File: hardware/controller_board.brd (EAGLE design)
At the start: 86 x 70 mm, 94 parts, among them J1 USB-MICROA-AMPHENOL-10118192-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, J2 2.4K, J3 2.4K, J4 AVR_SPI_PRG_6-SMD, J7 FRSKY-GIMBAL-2X-SERVO-SMD, J8 FRSKY-GIMBAL-2X-SERVO-SMD, P1 TEST-POINT, P2 TEST-POINT, P3 TEST-POINT, P4 TEST-POINT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

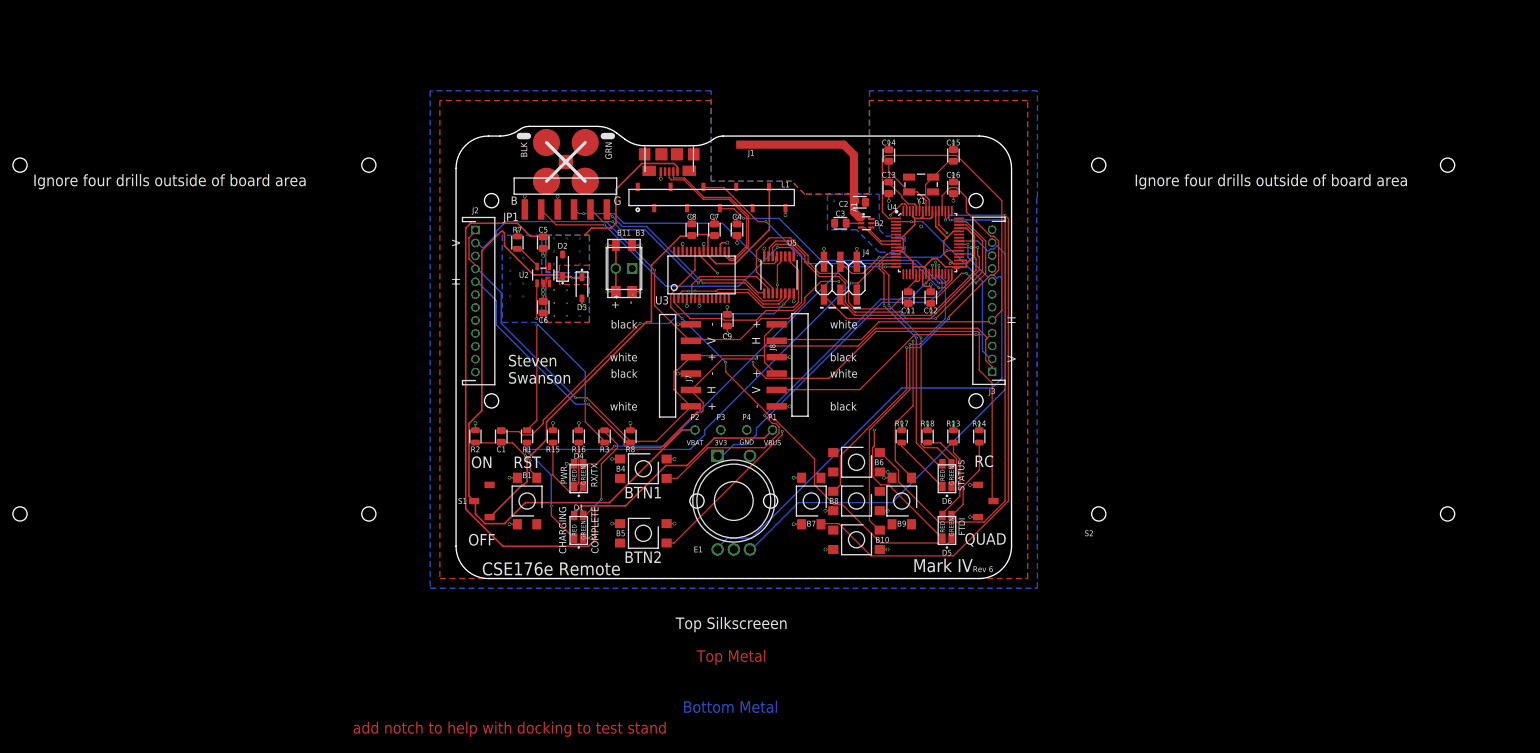
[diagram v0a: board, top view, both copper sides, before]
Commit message: reorg.  larger board.  More spacious.  Strain relief for the battery
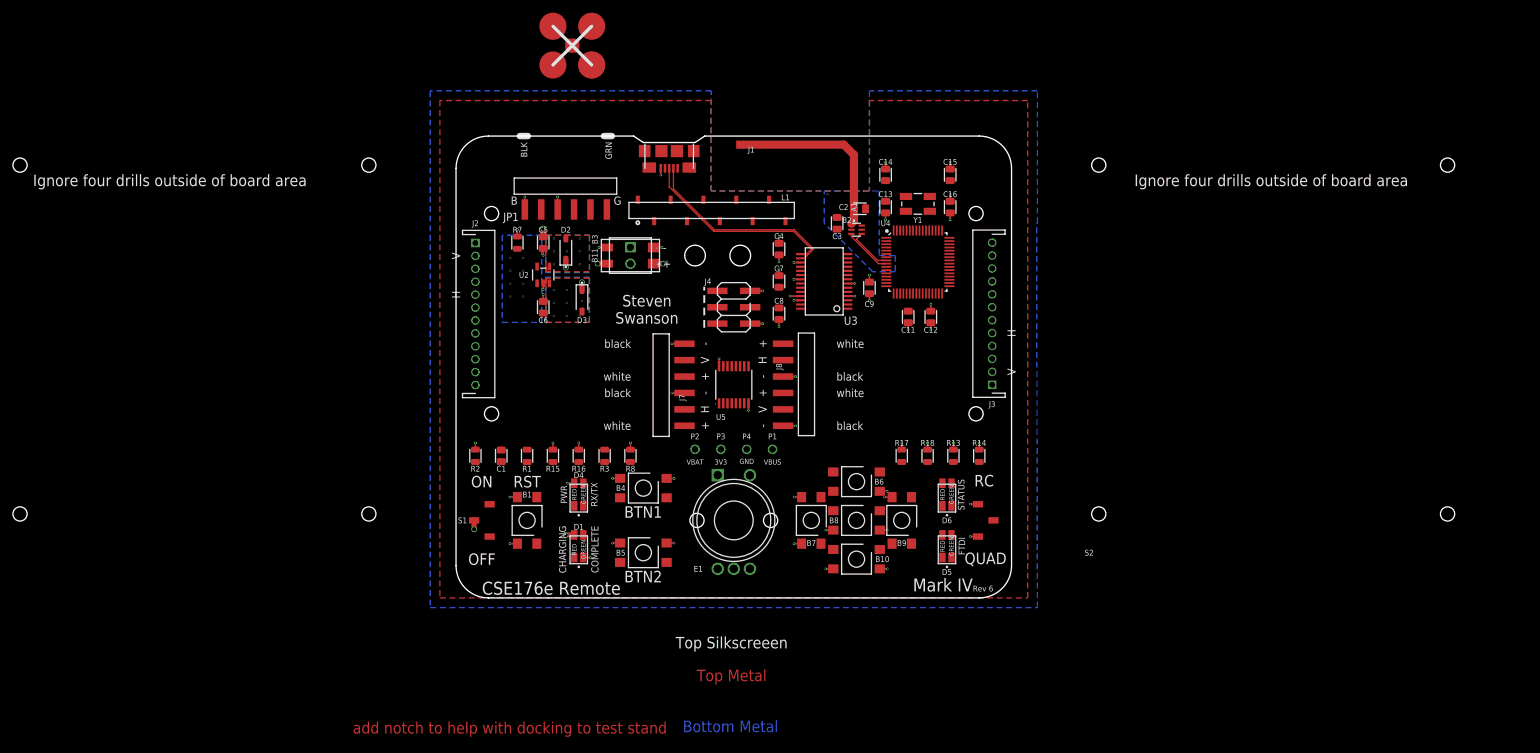
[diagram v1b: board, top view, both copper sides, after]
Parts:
- moved C9 22.6 mm to (21.0, 8.00)
- moved U3 19.0 mm to (14.0, 9.00), turned to 90 degrees
- moved C8 18.7 mm to (7.00, 4.00), turned to 270 degrees
- moved U5 18.4 mm to (0.00, -7.00), turned to 90 degrees
- moved U$134 18.0 mm to (-25.0, 45.5)
- moved J4 17.1 mm to (0.00, 5.00), turned to 270 degrees
- moved C7 12.8 mm to (7.00, 9.00)
- moved C4 7.16 mm to (7.00, 14.0)
- moved U$4 4.00 mm to (-46.1, 15.5)
- moved U$5 4.00 mm to (-43.0, 5.00)
- moved V10 3.81 mm to (-23.5, 6.00)
- moved U4 3.35 mm to (28.5, 12.0)
- moved J7 3.16 mm to (-7.00, -7.00)
- moved J8 3.16 mm to (7.00, -7.00)
- moved C13 3.04 mm to (23.5, 20.5)
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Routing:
- net VBUS: track 144.3 -> 2.63 mm, vias 0 -> 2
- net GREF: track 130.5 -> 0.00 mm, vias 1 -> 0
- net YAW: track 102.4 -> 0.00 mm, vias 3 -> 0
- net VBAT: track 104.0 -> 3.80 mm, vias 0 -> 3
- net BTN_LEFT: track 90.1 -> 0.00 mm, vias 2 -> 0
- net THROTTLE: track 88.9 -> 0.00 mm, vias 3 -> 0
- net ROLL: track 86.2 -> 0.00 mm
- net PROG_SEL: track 86.0 -> 0.00 mm, vias 2 -> 0
- net RESET: track 86.0 -> 0.00 mm, vias 3 -> 0
- net VREG_IN: track 84.1 -> 0.00 mm
- net E1-A: track 81.0 -> 0.00 mm, vias 1 -> 0
- net BTN_UP: track 79.7 -> 0.00 mm, vias 2 -> 0
- net E1-B: track 79.3 -> 0.00 mm, vias 1 -> 0
- net TXLED: track 72.8 -> 0.00 mm, vias 2 -> 0
- net BTN_RIGHT: track 67.2 -> 0.00 mm, vias 2 -> 0
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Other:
- board size 86 x 70 mm -> 86 x 71.5 mm

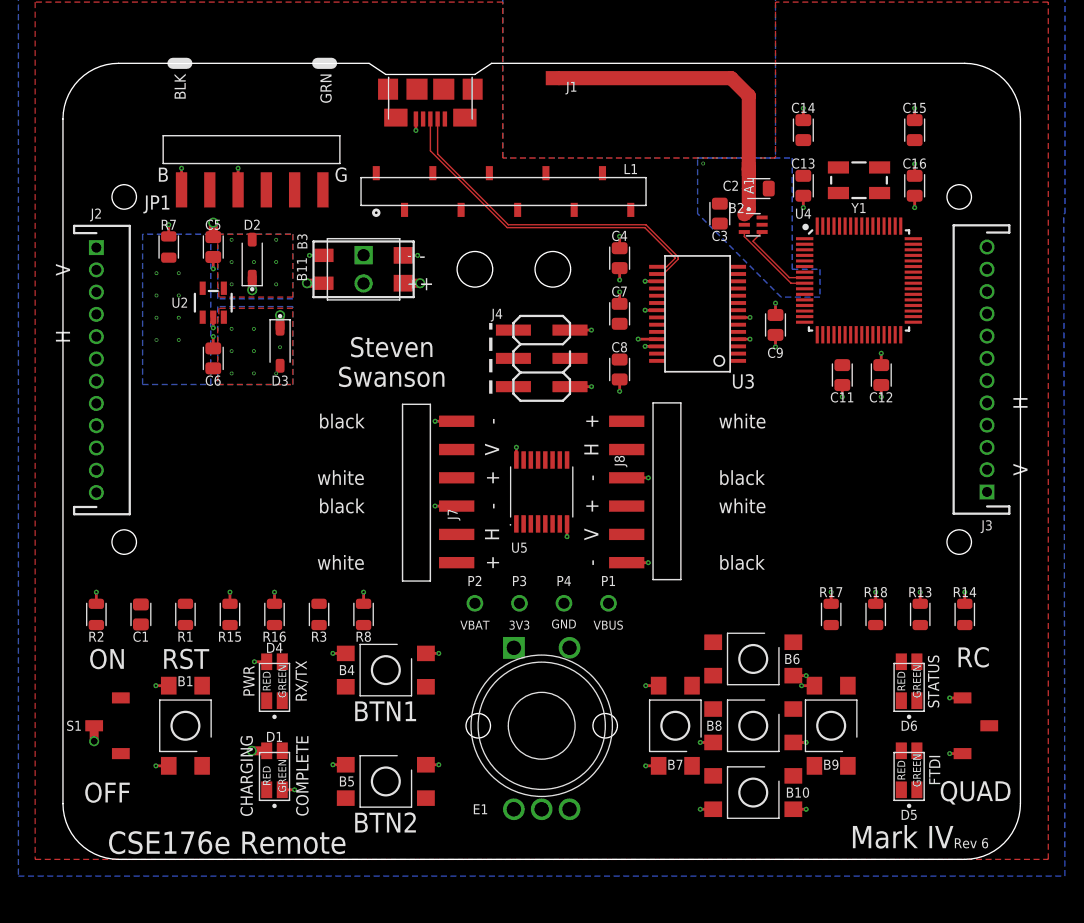
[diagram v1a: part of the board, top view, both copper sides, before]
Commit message: resolve meaningless merge
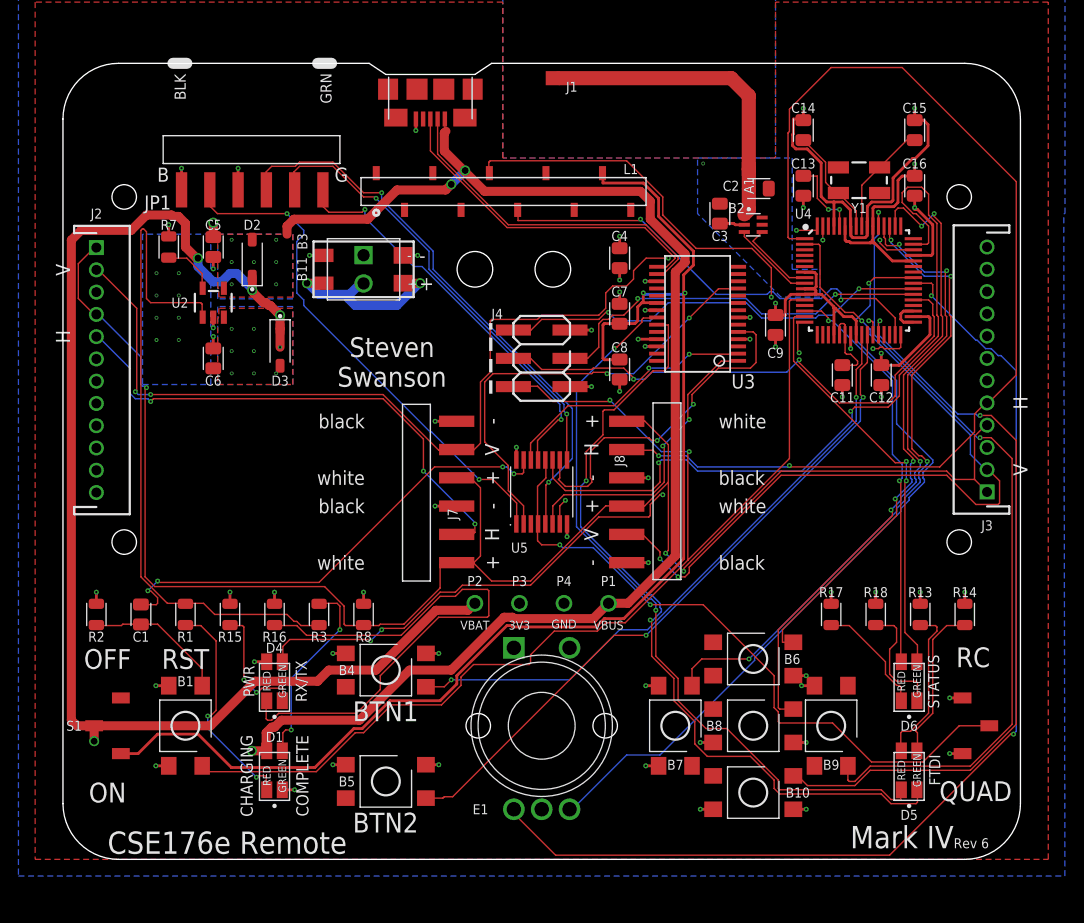
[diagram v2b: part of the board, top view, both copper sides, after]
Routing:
- net GREF: track 0.00 -> 156.3 mm, vias 0 -> 3
- net RESET: track 0.00 -> 122.3 mm, vias 0 -> 2
- net VBUS: track 2.63 -> 123.7 mm, vias 2 -> 4
- net VREG_IN: track 0.00 -> 117.2 mm, vias 0 -> 2
- net VBAT: track 3.80 -> 115.4 mm, vias 3 -> 4
- net E1-A: track 0.00 -> 97.3 mm, vias 0 -> 2
- net ROLL: track 0.00 -> 96.7 mm, vias 0 -> 2
- net THROTTLE: track 0.00 -> 93.0 mm, vias 0 -> 4
- net YAW: track 0.00 -> 89.9 mm, vias 0 -> 4
- net PITCH: track 0.00 -> 72.5 mm, vias 0 -> 3
- net TXLED: track 0.00 -> 72.3 mm, vias 0 -> 2
- net BTN_CENTER: track 0.00 -> 71.6 mm, vias 0 -> 2
- net E1-B: track 0.00 -> 70.4 mm, vias 0 -> 1
- net RXI-0: track 0.00 -> 69.3 mm, vias 0 -> 2
- net BTN_DOWN: track 0.00 -> 67.2 mm, vias 0 -> 2
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
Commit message: baby steps toward routabilty
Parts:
- moved V33 5.83 mm to (-26.9, 8.65)
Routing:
- net GND: track 120.8 -> 224.5 mm, vias 48 -> 45
- net N$13: track 50.0 -> 8.86 mm, vias 0 -> 2
- net BTN_RIGHT: track 56.7 -> 93.1 mm, vias 4 -> 2
- net BTN_LEFT: track 58.6 -> 93.7 mm, vias 4 -> 2
- net E1-A: track 97.3 -> 65.1 mm, vias 2 -> 1
- net BTN2/SDA: track 61.3 -> 87.8 mm
- net RXI-0: track 69.3 -> 45.4 mm
- net BTN_CENTER: track 71.6 -> 49.2 mm
- net GREF: track 156.3 -> 136.0 mm, vias 3 -> 4
- net VBUS: track 123.7 -> 104.2 mm, vias 4 -> 5
- net VREG_IN: track 117.2 -> 98.5 mm, vias 2 -> 1
- net CTS-1: track 46.4 -> 63.1 mm
- net PITCH: track 72.5 -> 56.2 mm, vias 3 -> 2
- net 3V3: track 45.1 -> 60.9 mm, vias 16 -> 14
- net RF: track 63.1 -> 77.2 mm, vias 4 -> 2
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
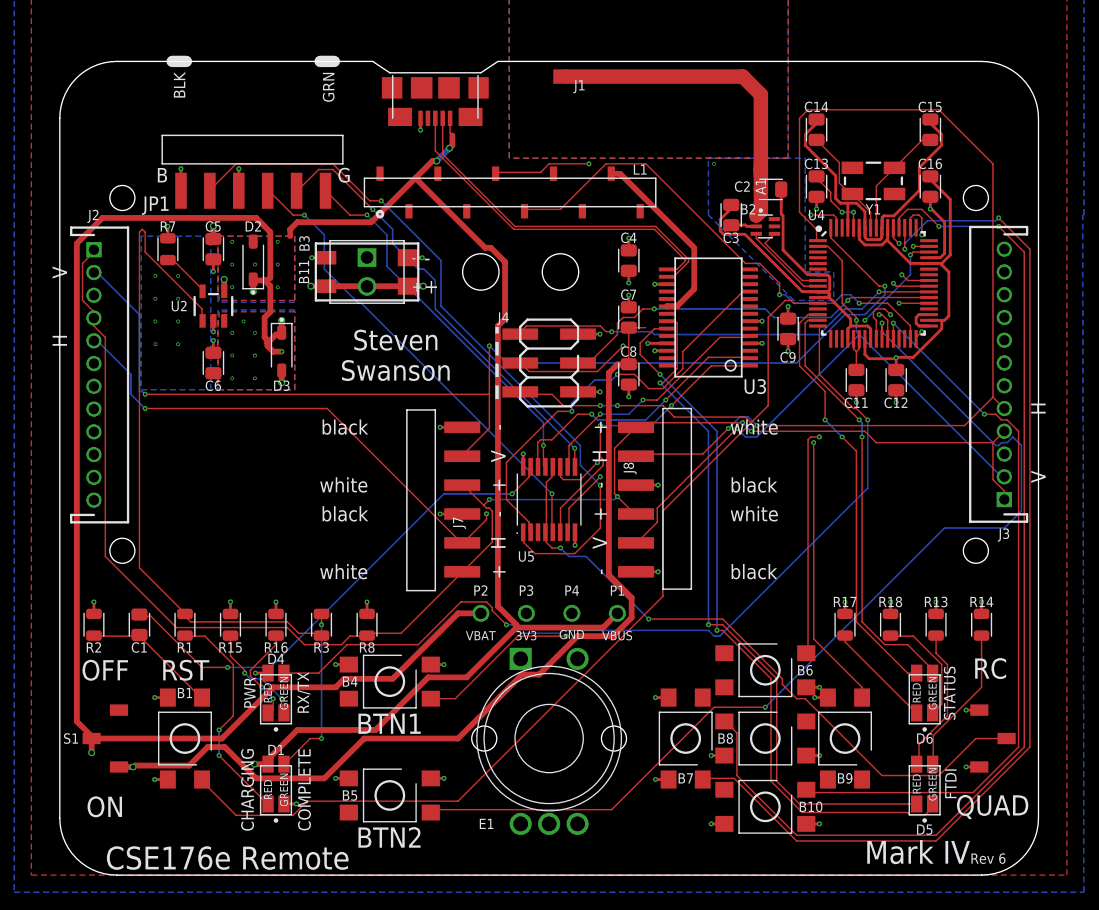
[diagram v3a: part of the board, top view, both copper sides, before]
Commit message: All routed with shield gnd to control routing
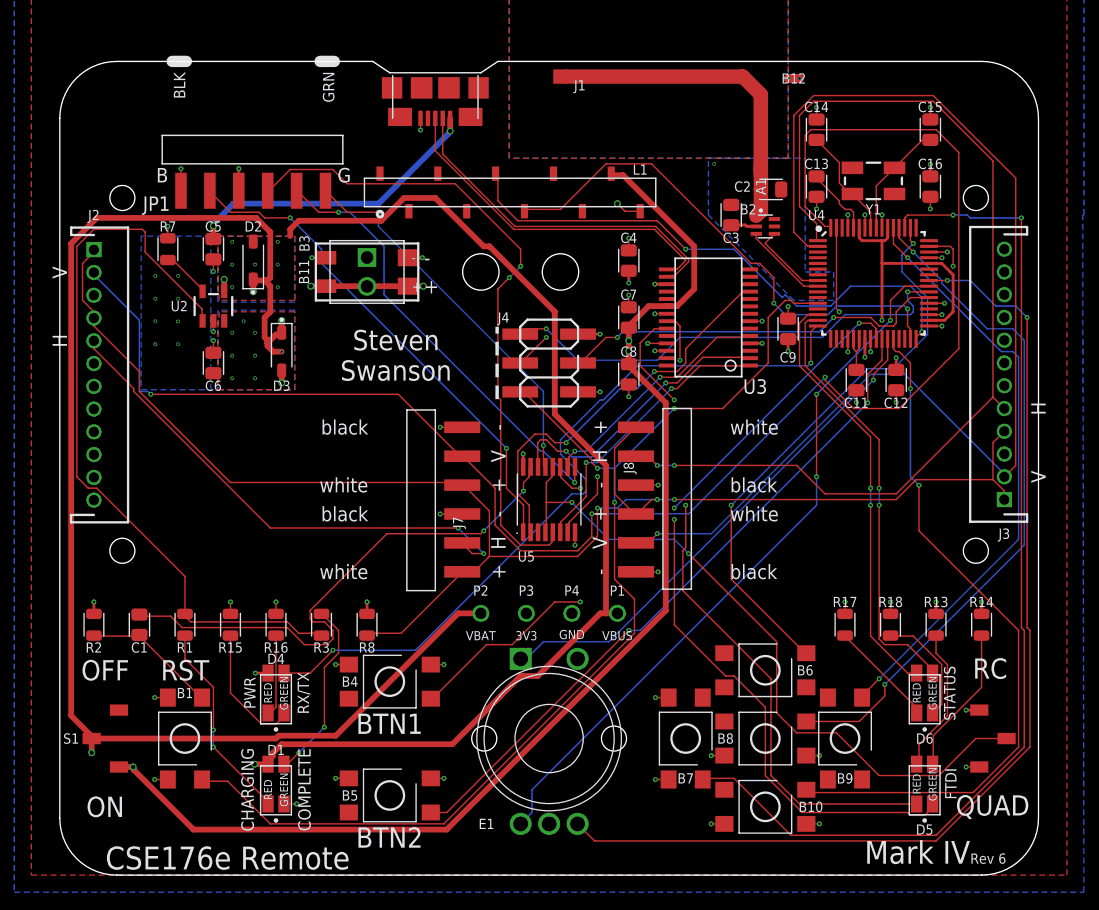
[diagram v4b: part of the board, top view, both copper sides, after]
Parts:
- added B12: NET_BRIDGE, custom:NET_BRIDGE
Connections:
- new net SHIELD: B12.P2
- net GND: now also B12.P1
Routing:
- net GND: track 224.5 -> 71.1 mm, vias 45 -> 55
- net PITCH: track 56.2 -> 105.1 mm, vias 2 -> 1
- net THROTTLE: track 99.9 -> 143.9 mm
- net BTN_RIGHT: track 93.1 -> 59.9 mm
- net BTN2/SDA: track 87.8 -> 59.4 mm
- net E1-B: track 64.5 -> 91.6 mm, vias 1 -> 2
- net CTS-1: track 63.1 -> 44.2 mm
- net VBUS: track 104.2 -> 122.9 mm, vias 5 -> 4
- net TXO-1: track 41.1 -> 57.3 mm
- net 3V3: track 60.9 -> 47.1 mm, vias 14 -> 17
- net RF: track 77.2 -> 67.0 mm
- net N$11: track 58.8 -> 66.3 mm
- net VREG_IN: track 98.5 -> 105.6 mm, vias 1 -> 3
- net TXO-0: track 46.1 -> 51.4 mm, vias 3 -> 2
- net BTN1/SCL: track 59.1 -> 53.9 mm, vias 2 -> 3
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
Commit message: bump version.  routed and decorated.
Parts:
- removed U$134: (no value), Artwork:QUADCLASS_LOGO
- added U$2: (no value), quadparts_prebuilt:QUADCLASS_LOGO_SMALL
- moved B10 1.00 mm to (19.0, -35.0)
- moved B6 1.00 mm to (19.0, -21.0)
- moved B12 0.50 mm to (21.5, 30.5)
- turned B9 to 270 degrees
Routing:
- net SHIELD: track 0.00 -> 69.1 mm
- net THROTTLE: track 143.9 -> 97.9 mm, vias 3 -> 2
- net BTN_LEFT: track 91.6 -> 54.0 mm
- net E1-B: track 91.6 -> 67.4 mm
- net RESET: track 111.6 -> 88.5 mm
- net PROG_SEL: track 61.4 -> 79.1 mm
- net BTN_DOWN: track 61.0 -> 48.3 mm
- net BTN_RIGHT: track 59.9 -> 47.7 mm
- net TXO-0: track 51.4 -> 63.3 mm
- net BTN2/SDA: track 59.4 -> 68.5 mm
- net PITCH: track 105.1 -> 96.1 mm
- net CTS-1: track 44.2 -> 52.8 mm
- net BTN1/SCL: track 53.9 -> 61.8 mm, vias 3 -> 2
- net ROLL: track 89.8 -> 82.6 mm, vias 2 -> 1
- net TXO-1: track 57.3 -> 50.1 mm
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
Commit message: restore shield
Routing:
- net SHIELD: track 69.1 -> 137.7 mm
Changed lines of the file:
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@@
 </signal>
 <signal name="SHIELD">
+<wire x1="21" y1="30.5" x2="21" y2="23" width="0.127" layer="2"/>
+<wire x1="21" y1="23" x2="22.5" y2="23" width="0.127" layer="2"/>
+<wire x1="22.5" y1="23" x2="22.5" y2="13" width="0.127" layer="2"/>
+<wire x1="22.5" y1="13" x2="25" y2="13" width="0.127" layer="2"/>
+<wire x1="25" y1="13" x2="25" y2="10.5" width="0.127" layer="2"/>
+<wire x1="25" y1="10.5" x2="21.5" y2="10.5" width="0.127" layer="2"/>
+<wire x1="21.5" y1="10.5" x2="14" y2="18" width="0.127" layer="2"/>
+<wire x1="14" y1="18" x2="14" y2="23" width="0.127" layer="2"/>
+<wire x1="14" y1="23" x2="-3.5" y2="23" width="0.127" layer="2"/>
+<wire x1="-3.5" y1="23" x2="-3.5" y2="31" width="0.127" layer="2"/>
 <wire x1="21" y1="31" x2="21" y2="23" width="0.127" layer="15"/>
 <wire x1="21" y1="23" x2="22.5" y2="23" width="0.127" layer="15"/>
@@
 <wire x1="-3.5" y1="23" x2="-3.5" y2="31" width="0.127" layer="15"/>
 <contactref element="B12" pad="P2"/>
-<wire x1="21" y1="31" x2="21" y2="30.5" width="0" layer="19" extent="1-15"/>
+<wire x1="21" y1="23" x2="21" y2="23" width="0" layer="19" extent="2-15"/>
 </signal>
 </signals>

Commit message: bump version.  routed and decorated.
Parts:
- removed U$1: (no value), RemoteParts:LAYER_LABELS
- added U$3: (no value), quadparts_prebuilt:LAYER_LABELS
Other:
- board text added: "FTDI RX"
- board text added: "FTDI TX"
- board text removed: "FTDI"
- board text removed: "add notch to help with docking to test stand"

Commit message: passes eaglint.
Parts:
- removed V10: LOCKED-VIA-0.2, quadparts_prebuilt:VIA-0.2MM
- moved U$4 29.2 mm to (-72.0, 2.00)
- moved R3 9.49 mm to (-29.0, -15.0)
- moved R15 7.62 mm to (-21.0, -15.0)
- moved D3 4.03 mm to (-24.0, 10.0)
- moved C15 3.81 mm to (32.0, 29.0)
- moved C16 3.81 mm to (32.0, 24.0)
- moved V3 3.63 mm to (-36.0, 16.0)
- moved V35 3.63 mm to (-34.0, 12.0)
- moved V37 3.63 mm to (-34.0, 14.0)
- moved V38 3.63 mm to (-36.0, 12.0)
- moved V4 3.63 mm to (-36.0, 10.0)
- moved V5 3.63 mm to (-34.0, 10.0)
- moved V7 3.63 mm to (-36.0, 14.0)
- moved V8 3.63 mm to (-34.0, 16.0)
- moved V30 3.54 mm to (-27.0, 9.00)
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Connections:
- removed net BAT_SENSE: U4.3
- net VBAT: no longer V10.P1
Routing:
- net GREF: track 133.2 -> 0.00 mm, vias 2 -> 0
- net VBAT: track 120.4 -> 0.00 mm, vias 3 -> 0
- net VBUS: track 117.8 -> 0.00 mm, vias 4 -> 0
- net VREG_IN: track 104.9 -> 0.00 mm, vias 3 -> 0
- net THROTTLE: track 97.9 -> 0.00 mm, vias 2 -> 0
- net PITCH: track 96.1 -> 0.00 mm, vias 1 -> 0
- net YAW: track 91.9 -> 0.00 mm, vias 2 -> 0
- net RESET: track 88.5 -> 0.00 mm, vias 3 -> 0
- net ROLL: track 82.6 -> 0.00 mm, vias 1 -> 0
- net PROG_SEL: track 79.1 -> 0.00 mm, vias 2 -> 0
- net GND: track 74.5 -> 0.00 mm, vias 59 -> 0
- net RF: track 69.4 -> 0.00 mm, vias 2 -> 0
- net BTN2/SDA: track 68.5 -> 0.00 mm, vias 2 -> 0
- net E1-A: track 67.4 -> 0.00 mm, vias 2 -> 0
- net E1-B: track 67.4 -> 0.00 mm, vias 2 -> 0
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- added copper zone on layer 16, net VBAT
- added copper zone on layer 16, net VREG_IN
- removed copper zone on layer 16, net 3V3
